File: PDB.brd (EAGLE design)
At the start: 130.3 x 166.9 mm, 49 parts, among them J1 B06B-HCMKK, J2 B06B-HCMKK, J3 SS-6488-NF-A431, J4 SS-6488-NF-A431, J5 B06B-HCMKK, J6 B03B-HCMKS, J7 B03B-HCMKS, J8 SS-6488-NF-A431

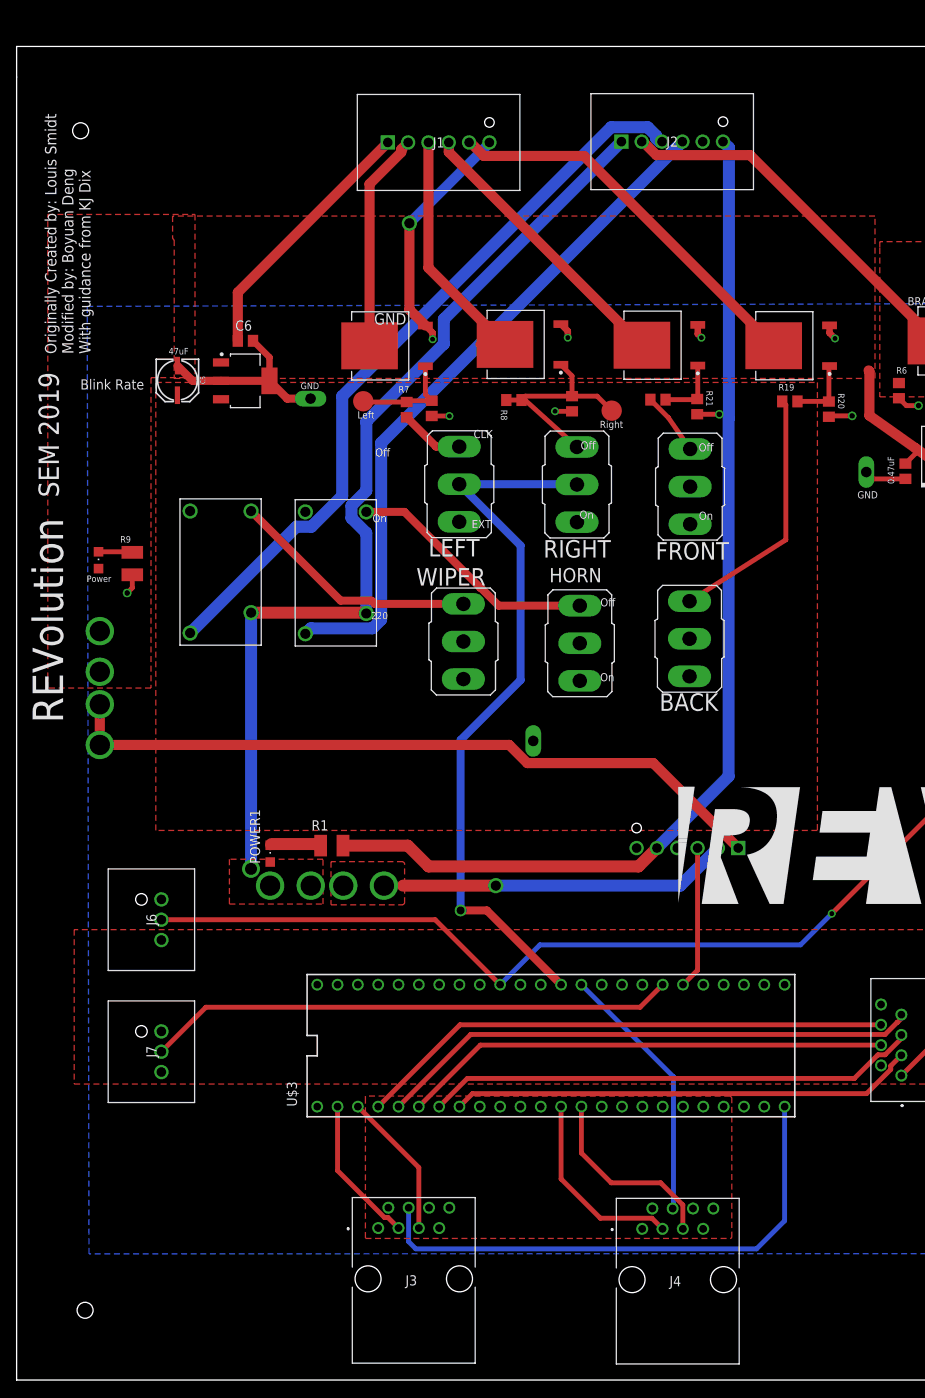
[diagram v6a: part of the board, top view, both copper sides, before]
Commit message: Added voltage divider so that Teensy 3.5 sees Wiper and Horn are turned on
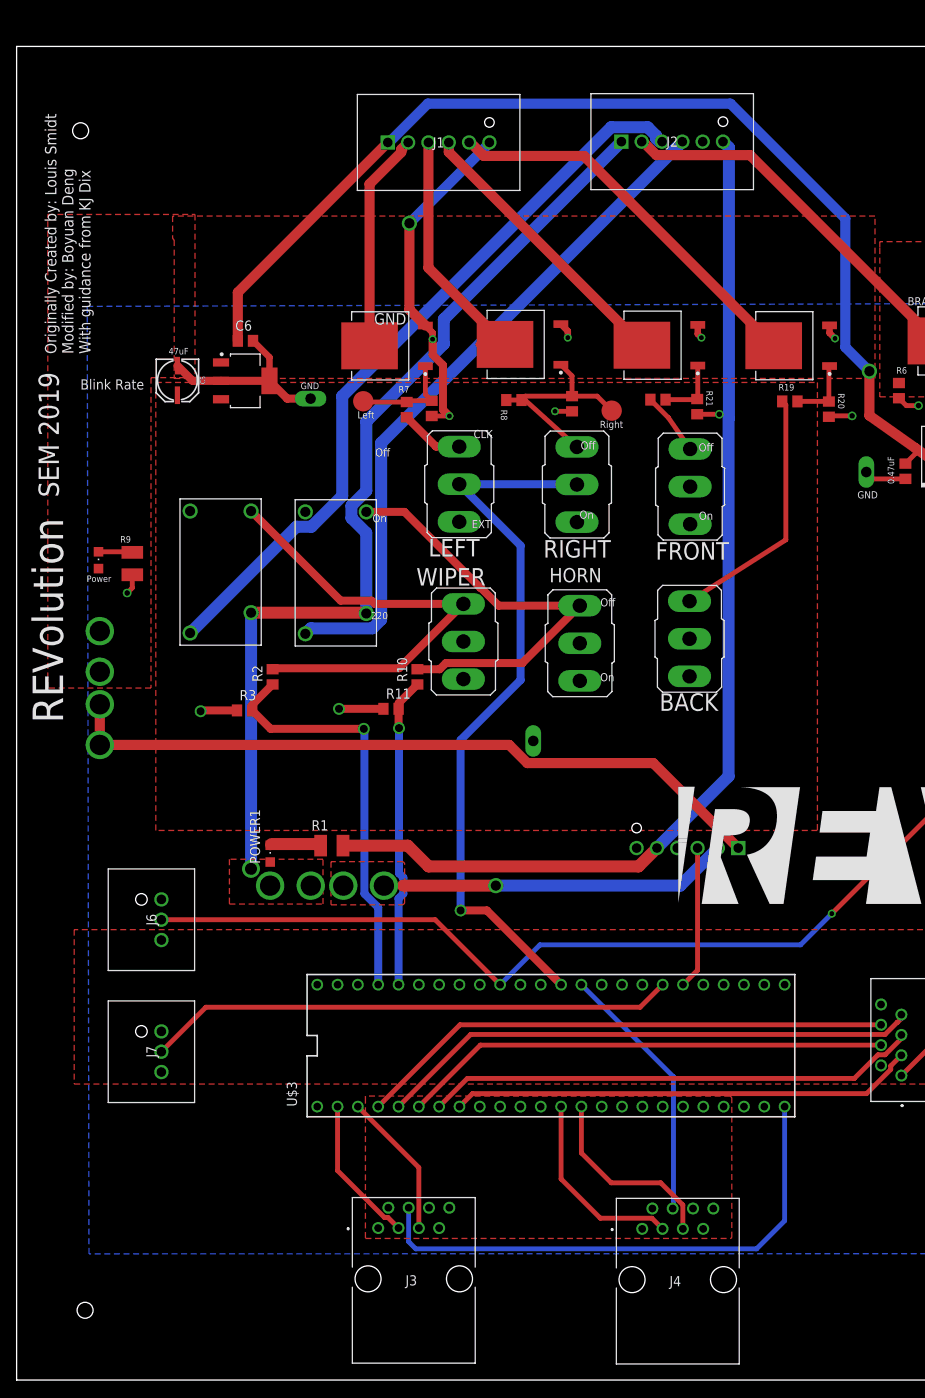
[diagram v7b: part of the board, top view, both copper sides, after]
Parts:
- added R10, R2: 3K, master_library:R0805
- added R11, R3: 5K, master_library:R0805
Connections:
- new net HORN_IN: R10.1, R11.2, U$3.22
- new net WIPER_IN: R2.1, R3.2, U$3.23
- net GND: now also R11.1, R3.1
- net H4: now also R2.2
- net H9: now also R10.2
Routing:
- net VDD: track 52.6 -> 138.1 mm, vias 0 -> 1
- net WIPER_IN: track 0.00 -> 51.9 mm, vias 0 -> 1
- net HORN_IN: track 0.00 -> 39.0 mm, vias 0 -> 1
- net H4: track 31.3 -> 58.6 mm
- net H9: track 31.5 -> 55.1 mm
- net GND: track 86.6 -> 107.2 mm, vias 12 -> 14
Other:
- outline, holes or cut-outs redrawn
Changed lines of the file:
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@@
 <text x="20.9" y="116.1" size="0.8128" layer="25">47uF</text>
 <text x="111.6" y="99.9" size="0.8128" layer="25" rot="R90">0.47uF</text>
-<wire x1="1.9" y1="150.8" x2="1.9" y2="150.7" width="0.1524" layer="20"/>
-<wire x1="1.9" y1="150.7" x2="1.9" y2="-12.1" width="0.1524" layer="20"/>
+<wire x1="1.9" y1="154.6" x2="1.9" y2="-12.1" width="0.1524" layer="20"/>
 <wire x1="1.9" y1="-12.1" x2="132" y2="-12.1" width="0.1524" layer="20"/>
 <wire x1="132" y1="-12.1" x2="132.2" y2="-12.3" width="0.1524" layer="20"/>
 <wire x1="132.2" y1="-12.3" x2="132.2" y2="154.6" width="0.1524" layer="20"/>
 <wire x1="132.2" y1="154.6" x2="1.9" y2="154.6" width="0.1524" layer="20"/>
-<wire x1="1.9" y1="154.6" x2="1.9" y2="150.8" width="0.1524" layer="20"/>
 </plain>
 <attributes>
@@
 <attribute name="VALUE" x="119.0352" y="30.0922" size="1.27" layer="27" rot="R90" align="center"/>
 </element>
+<element name="R2" library="master_library" package="R0805" package3d_urn="urn:adsk.eagle:package:2274104/1" value="3K" x="33.9" y="75.8" smashed="yes" rot="R90">
+<attribute name="NAME" x="32.63" y="75.165" size="1.27" layer="25" rot="R90"/>
+<attribute name="VALUE" x="36.44" y="75.165" size="1.27" layer="27" rot="R90"/>
+</element>
+<element name="R3" library="master_library" package="R0805" package3d_urn="urn:adsk.eagle:package:2274104/1" value="5K" x="30.4" y="71.6" smashed="yes">
+<attribute name="NAME" x="29.765" y="72.87" size="1.27" layer="25"/>
+<attribute name="VALUE" x="29.765" y="69.06" size="1.27" layer="27"/>
+</element>
+<element name="R10" library="master_library" package="R0805" package3d_urn="urn:adsk.eagle:package:2274104/1" value="3K" x="52" y="75.8" smashed="yes" rot="R90">
+<attribute name="NAME" x="50.73" y="75.165" size="1.27" layer="25" rot="R90"/>
+<attribute name="VALUE" x="54.54" y="75.165" size="1.27" layer="27" rot="R90"/>
+</element>
+<element name="R11" library="master_library" package="R0805" package3d_urn="urn:adsk.eagle:package:2274104/1" value="5K" x="48.7" y="71.8" smashed="yes">
+<attribute name="NAME" x="48.065" y="73.07" size="1.27" layer="25"/>
+<attribute name="VALUE" x="48.065" y="69.26" size="1.27" layer="27"/>
+</element>
 </elements>
 <signals>
@@
 <wire x1="29.55" y1="117.8" x2="29.55" y2="123.85" width="1.27" layer="1"/>
 <wire x1="29.55" y1="123.85" x2="48.3" y2="142.6" width="1.27" layer="1"/>
+<via x="108.5" y="114" extent="1-16" drill="1.27"/>
+<wire x1="48.3" y1="142.6" x2="48.45365" y2="142.6" width="1.27" layer="16"/>
+<wire x1="105.4906" y1="117.0094" x2="108.5" y2="114" width="1.27" layer="16"/>
+<wire x1="91.1324" y1="147.451" x2="105.4906" y2="133.0928" width="1.27" layer="16"/>
+<wire x1="105.4906" y1="133.0928" x2="105.4906" y2="117.0094" width="1.27" layer="16"/>
+<wire x1="48.45365" y1="142.6" x2="53.30465" y2="147.451" width="1.27" layer="16"/>
+<wire x1="53.30465" y1="147.451" x2="91.1324" y2="147.451" width="1.27" layer="16"/>
 </signal>
 <signal name="HAZ_L_SIG">
@@
 <wire x1="31.21" y1="96.52" x2="42.4051" y2="85.3249" width="1" layer="1"/>
 <wire x1="42.4051" y1="85.3249" x2="46.274775" y2="85.3249" width="1" layer="1"/>
+<contactref element="R2" pad="2"/>
+<wire x1="33.9" y1="76.87" x2="33.9" y2="76.75" width="1" layer="1"/>
+<wire x1="57.748" y1="84.918" x2="49.7" y2="76.87" width="1" layer="1"/>
+<wire x1="49.7" y1="76.87" x2="33.9" y2="76.87" width="1" layer="1"/>
 </signal>
 <signal name="H7">
@@
 <contactref element="C5" pad="+"/>
 <contactref element="HORN" pad="2"/>
+<wire x1="72.3" y1="80" x2="57.748" y2="80.219" width="0" layer="19" extent="1-1"/>
 </signal>
 <signal name="GND">
@@
 <wire x1="51" y1="132.5" x2="61" y2="142.5" width="1.27" layer="16"/>
 <wire x1="61" y1="142.5" x2="61" y2="142.6" width="1.27" layer="16"/>
-<wire x1="53.9" y1="118" x2="53.792" y2="108.4078125" width="0" layer="19" extent="1-1"/>
+<wire x1="53.9" y1="118" x2="53.9" y2="116.0653125" width="1" layer="1"/>
+<wire x1="55.1944" y1="109.2056" x2="55.9921875" y2="108.4078125" width="1" layer="1"/>
+<wire x1="53.9" y1="116.0653125" x2="55.1944" y2="114.7709125" width="1" layer="1"/>
+<wire x1="55.1944" y1="114.7709125" x2="55.1944" y2="109.2056" width="1" layer="1"/>
+<contactref element="R3" pad="1"/>
+<contactref element="R11" pad="1"/>
+<wire x1="29.45" y1="71.6" x2="25" y2="71.6" width="1" layer="1"/>
+<wire x1="25" y1="71.6" x2="24.9" y2="71.5" width="1" layer="1"/>
+<via x="24.9" y="71.5" extent="1-16" drill="1"/>
+<wire x1="47.75" y1="71.8" x2="42.2" y2="71.8" width="1" layer="1"/>
+<via x="42.2" y="71.8" extent="1-16" drill="1"/>
 </signal>
 <signal name="AGND">
@@
 <via x="61.8" y="49.7" extent="1-16" drill="1.27"/>
 <wire x1="61.8" y1="49.7" x2="50.2" y2="49.7" width="1.5" layer="1"/>
-<wire x1="47.812" y1="49.7" x2="50.2" y2="49.7" width="0" layer="19" extent="1-1"/>
-<wire x1="42.732" y1="49.7" x2="47.812" y2="49.7" width="0" layer="19" extent="1-1"/>
 </signal>
 <signal name="IGND">
@@
 <wire x1="59.93103125" y1="86.92295" x2="62.15498125" y2="84.699" width="1" layer="1"/>
 <wire x1="50.38" y1="96.42" x2="59.87705" y2="86.92295" width="1" layer="1"/>
+<contactref element="R10" pad="2"/>
+<wire x1="55.56496875" y1="77.52495" x2="54.79001875" y2="76.75" width="1" layer="1"/>
+<wire x1="54.79001875" y1="76.75" x2="52" y2="76.75" width="1" layer="1"/>
+<wire x1="72.3" y1="84.699" x2="65.12595" y2="77.52495" width="1" layer="1"/>
+<wire x1="65.12595" y1="77.52495" x2="55.56496875" y2="77.52495" width="1" layer="1"/>
 </signal>
 <signal name="WIPER">
@@
 <wire x1="58.88" y1="23.7" x2="108.14160625" y2="23.7" width="0.6096" layer="1"/>
 </signal>
+<signal name="WIPER_IN">
+<contactref element="U$3" pad="23"/>
+<contactref element="R2" pad="1"/>
+<contactref element="R3" pad="2"/>
+<wire x1="33.9" y1="74.85" x2="31.35" y2="72.3" width="1" layer="1"/>
+<wire x1="31.35" y1="72.3" x2="31.35" y2="71.6" width="1" layer="1"/>
+<via x="45.3" y="69.3" extent="1-16" drill="1"/>
+<wire x1="45.3" y1="69.3" x2="45.3816" y2="69.2184" width="1" layer="16"/>
+<wire x1="45.3816" y1="69.2184" x2="45.3816" y2="48.69329375" width="1" layer="16"/>
+<wire x1="47.1" y1="46.97489375" x2="47.1" y2="37.32" width="1" layer="16"/>
+<wire x1="45.3816" y1="48.69329375" x2="47.1" y2="46.97489375" width="1" layer="16"/>
+<wire x1="31.35" y1="71.6" x2="33.65" y2="69.3" width="1" layer="1"/>
+<wire x1="33.65" y1="69.3" x2="45.3" y2="69.3" width="1" layer="1"/>
+</signal>
+<signal name="HORN_IN">
+<contactref element="U$3" pad="22"/>
+<contactref element="R10" pad="1"/>
+<contactref element="R11" pad="2"/>
+<wire x1="52" y1="74.85" x2="49.65" y2="72.5" width="1" layer="1"/>
+<wire x1="49.65" y1="72.5" x2="49.65" y2="71.8" width="1" layer="1"/>
+<wire x1="49.65" y1="71.8" x2="49.65" y2="69.45" width="1" layer="1"/>
+<wire x1="49.65" y1="69.45" x2="49.7" y2="69.4" width="1" layer="1"/>
+<via x="49.7" y="69.4" extent="1-16" drill="1"/>
+<wire x1="49.7" y1="69.4" x2="49.7" y2="51.24910625" width="1" layer="16"/>
+<wire x1="49.7" y1="51.24910625" x2="50.2424" y2="50.70670625" width="1" layer="16"/>
+<wire x1="50.2424" y1="50.70670625" x2="50.2424" y2="48.69329375" width="1" layer="16"/>
+<wire x1="49.64" y1="48.09089375" x2="49.64" y2="37.32" width="1" layer="16"/>
+<wire x1="50.2424" y1="48.69329375" x2="49.64" y2="48.09089375" width="1" layer="16"/>
+</signal>
 </signals>

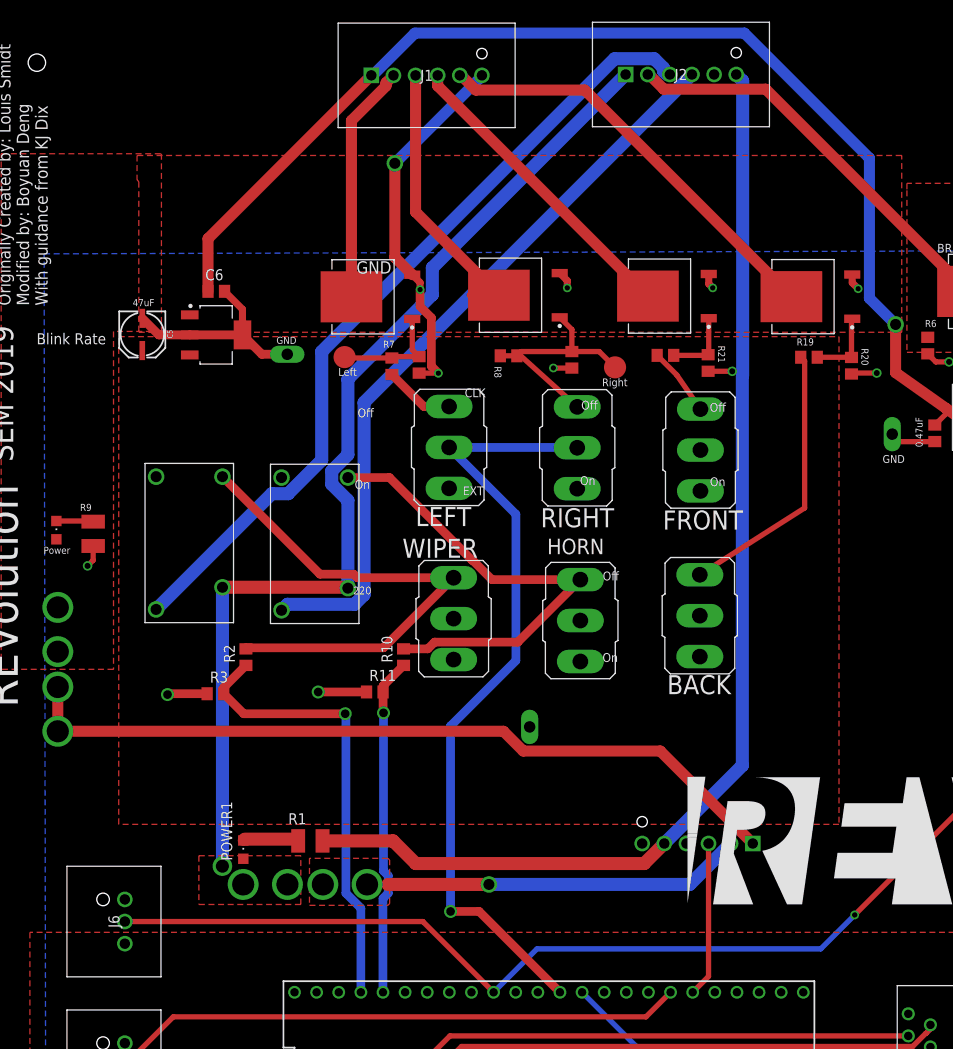
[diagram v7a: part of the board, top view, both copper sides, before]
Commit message: With diode, pass signal direcely to ISOENABLE
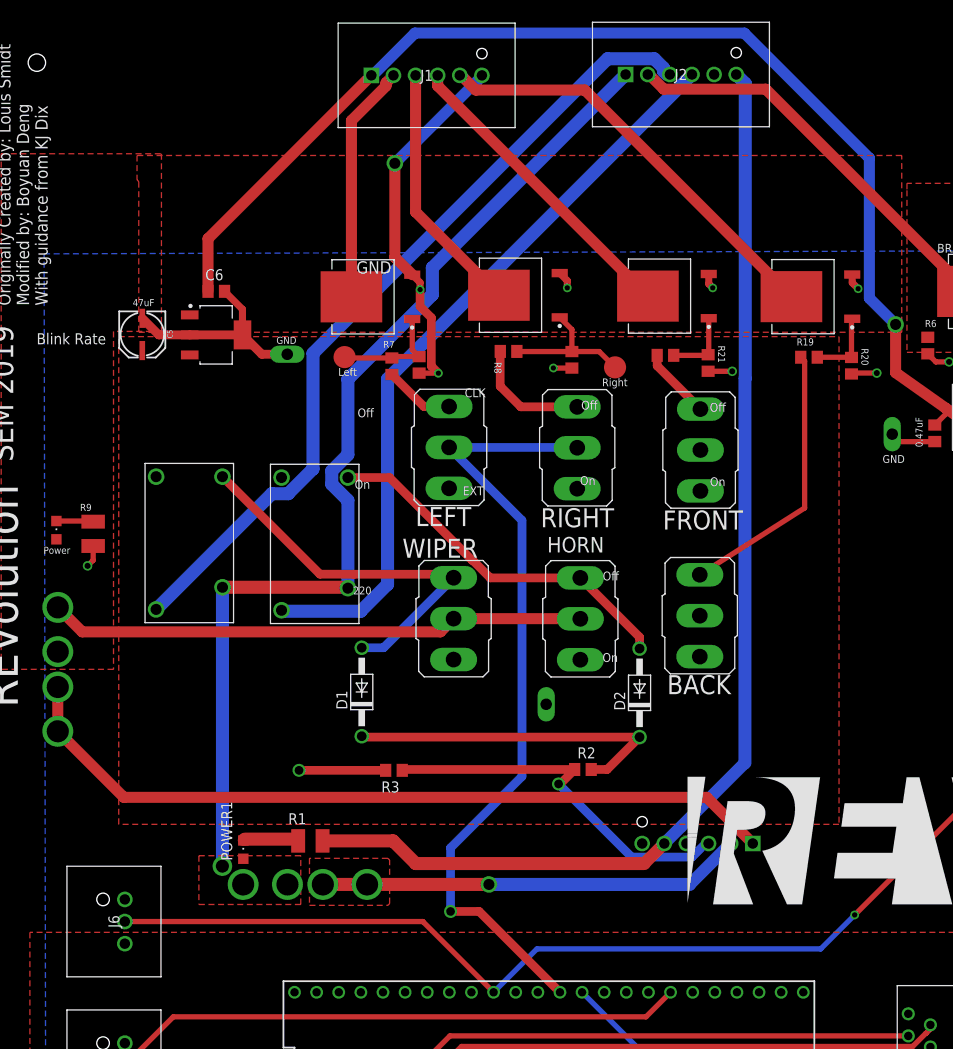
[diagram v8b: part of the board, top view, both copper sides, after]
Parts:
- removed R10: 3K, master_library:R0805
- removed R11: 5K, master_library:R0805
- added D1, D2: 1N4004, diode:DO41-10
- R2: value 3K -> 4K
- R3: value 5K -> 4K
- moved R2 40.8 mm to (72.6, 62.9), turned to 0 degrees
- moved R3 22.3 mm to (50.9, 62.8), turned to 180 degrees
- moved TP11 3.22 mm to (68.4, 70.4)
- moved R8 0.50 mm to (64.1, 110.9)
- moved HORN 0.20 mm to (72.3, 80.2)
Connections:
- removed net HORN_IN: R10.1, R11.2, U$3.22
- removed net WIPER_IN: R2.1, R3.2, U$3.23
- new net N$3: D1.C, D2.C, R2.2
- net 10V_REG: no longer HORN.2, WIPER.2
- net GND: now also R3.2; no longer R11.1, R3.1
- net H4: now also D1.A; no longer R2.2
- net H9: now also D2.A; no longer R10.2
- net ISOENABLE: now also R2.1, R3.1; no longer U$3.38
- net VDD: now also HORN.2, WIPER.2
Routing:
- net VDD: track 138.1 -> 199.8 mm
- net WIPER_IN: track 51.9 -> 0.00 mm, vias 1 -> 0
- net N$3: track 0.00 -> 39.0 mm
- net HORN_IN: track 39.0 -> 0.00 mm, vias 1 -> 0
- net ISOENABLE: track 17.8 -> 43.7 mm, vias 0 -> 1
- net H4: track 58.6 -> 45.2 mm
- net H9: track 55.1 -> 42.4 mm
- net N$8: track 41.3 -> 48.8 mm
- net HAZ_R_SIG: track 32.5 -> 29.2 mm
- net H2: track 11.1 -> 13.8 mm
- net HORN: track 85.6 -> 86.5 mm
- net CLK: track 90.7 -> 91.3 mm
- net GND: track 107.2 -> 107.0 mm, vias 14 -> 13
